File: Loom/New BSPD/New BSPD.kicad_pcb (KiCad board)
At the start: 2 copper layers, 148.6 x 83.8 mm, 54 parts, among them J1 Conn_01x03, J2 Conn_01x03, J3 Conn_01x03, J4 Screw_Terminal_01x02, K1 MCCMA51-S-DC12V-C, Q1 IRLZ44Z, U1 4011, U10 LM2901, U11 4012, U12 74LS573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

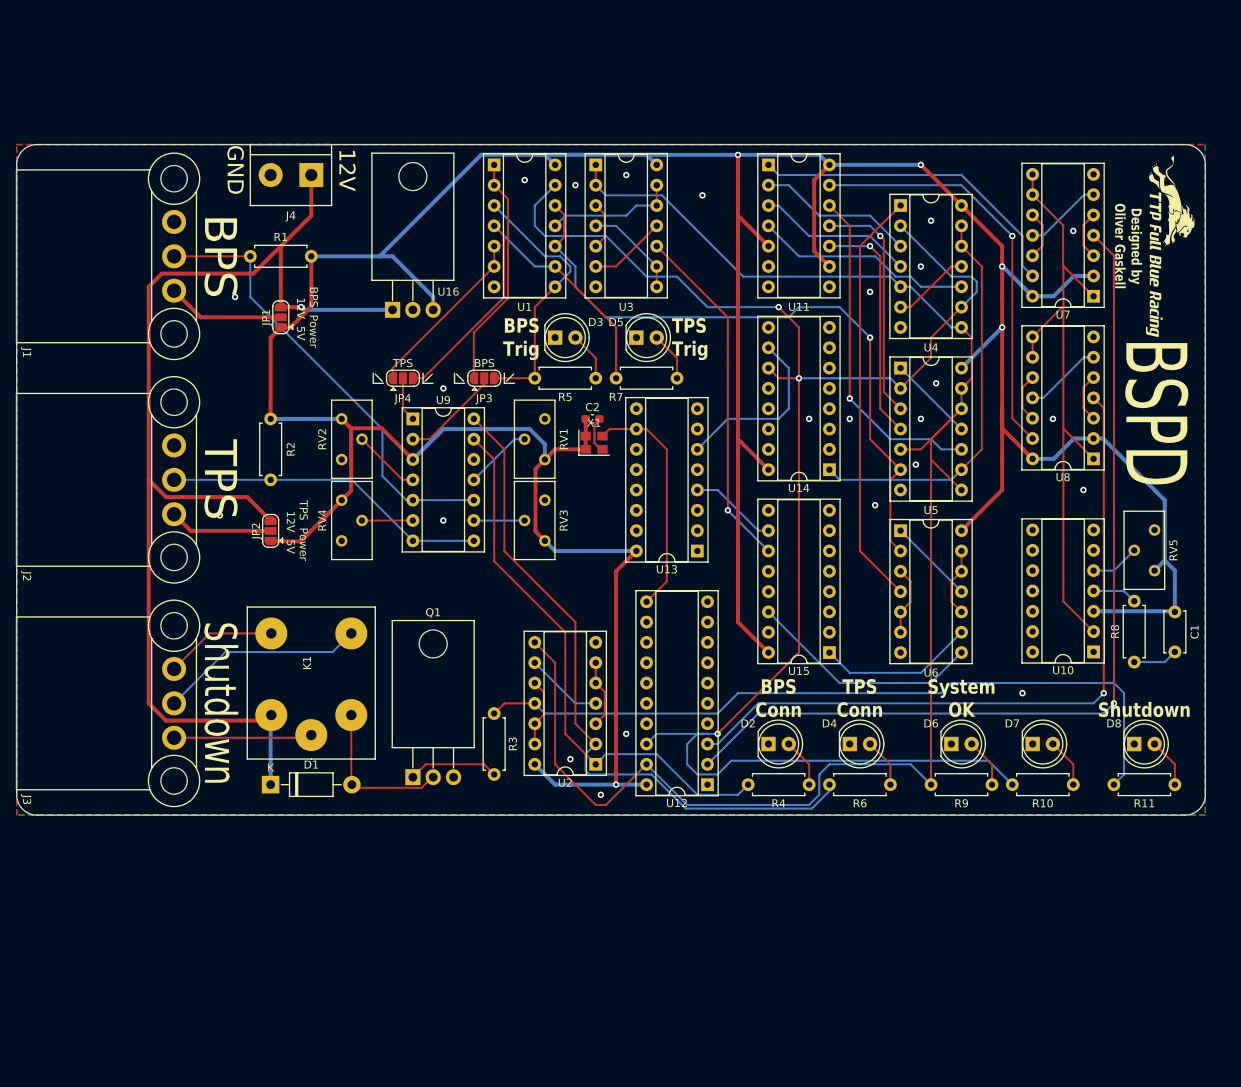
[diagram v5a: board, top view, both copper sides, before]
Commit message: Add mounting holes
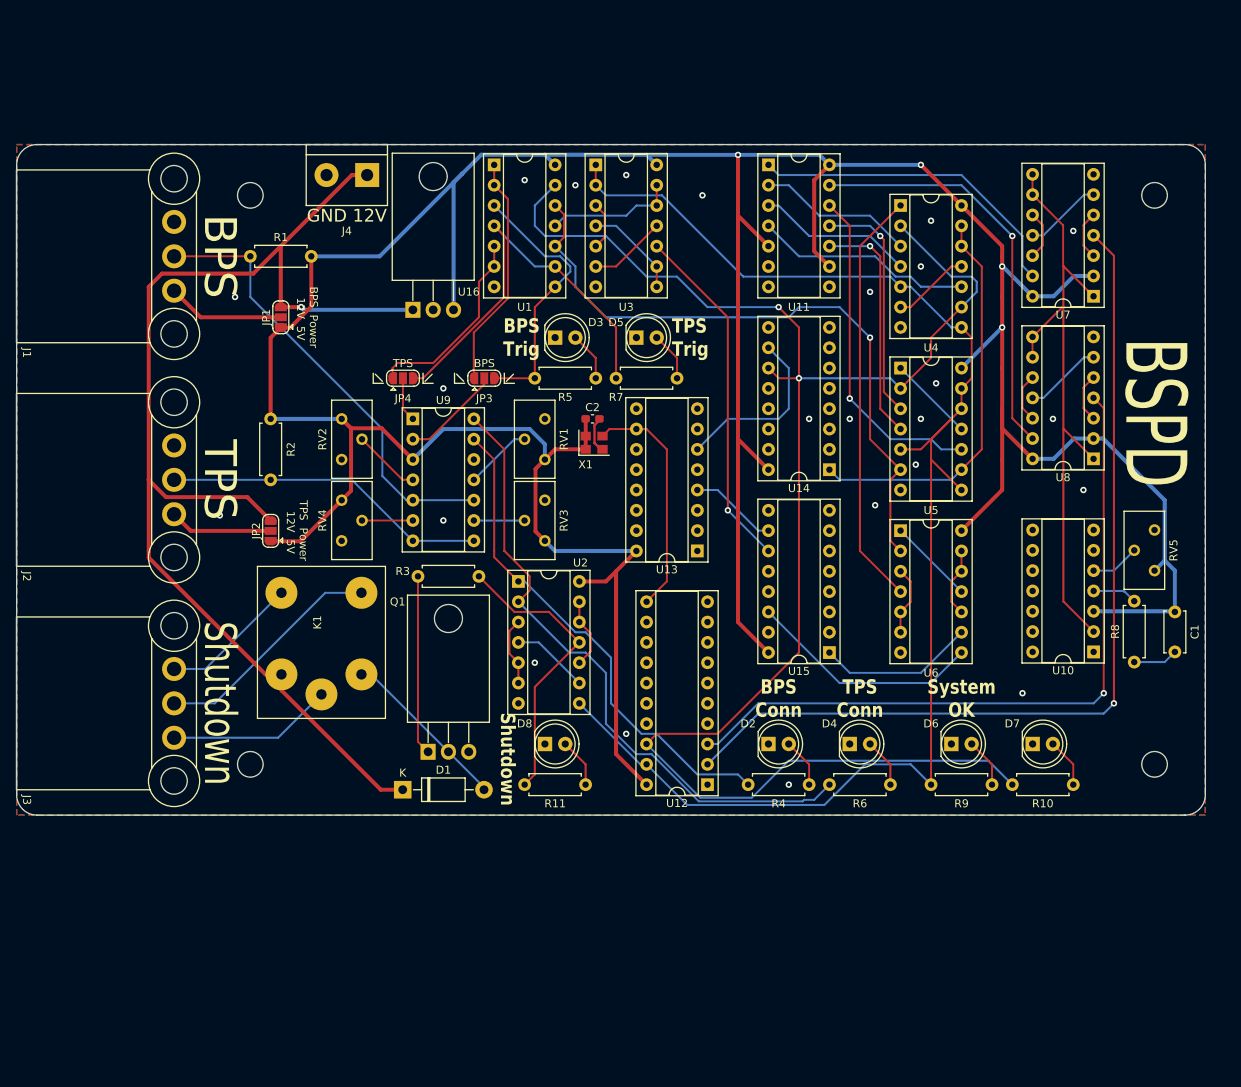
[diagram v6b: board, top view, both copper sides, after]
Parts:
- added MNT1: MountingHole_3.2mm_M3, MountingHole:MountingHole_3.2mm_M3, F.Cu at (194.3, 29.2)
- added MNT2: MountingHole_3.2mm_M3, MountingHole:MountingHole_3.2mm_M3, F.Cu at (194.3, 100.3)
- added MNT3: MountingHole_3.2mm_M3, MountingHole:MountingHole_3.2mm_M3, F.Cu at (81.3, 29.2)
- added MNT4: MountingHole_3.2mm_M3, MountingHole:MountingHole_3.2mm_M3, F.Cu at (81.3, 100.3)
- G***: moved to B.Cu
- moved D8 73.7 mm to (118.1, 97.8)
- moved R11 73.7 mm to (123.2, 102.9)
- moved U2 24.8 mm to (114.8, 77.5), turned to 0 degrees
- moved R3 17.3 mm to (109.9, 76.8), turned to 180 degrees
- moved D1 16.5 mm to (100.3, 103.5)
- moved G*** 16.1 mm to (191.8, 50.8)
- moved J4 6.98 mm to (95.9, 26.7)
- moved K1 5.24 mm to (90.2, 91.6)
- moved Q1 3.70 mm to (103.5, 98.8)
- moved U16 2.54 mm to (101.6, 43.5)
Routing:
- net /SD_Sig: track 93.9 -> 36.6 mm
- net /SM_Ok: track 203.0 -> 181.1 mm
- net Net-(Q1-G): track 11.4 -> 22.5 mm
- net +12V: track 146.0 -> 153.5 mm
- net /BPS_Plugged: track 69.2 -> 62.7 mm
- net /TPS_Plugged: track 85.0 -> 80.1 mm
- net /ShutdownNO: track 14.0 -> 17.4 mm
- net /ShutdownNC: track 25.8 -> 29.1 mm
- net /ShutdownC: track 17.3 -> 20.7 mm
- net /State Machine/State_B: track 204.8 -> 207.8 mm, vias 3 -> 2
- net Net-(JP4-A): track 21.8 -> 24.4 mm
- net Net-(D1-A): track 19.6 -> 21.5 mm
- net +5V: track 476.5 -> 475.2 mm, vias 5 -> 4
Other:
- board text added: "GND 12V"
- board text removed: "12V"
- board text removed: "GND"

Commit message: Add test points
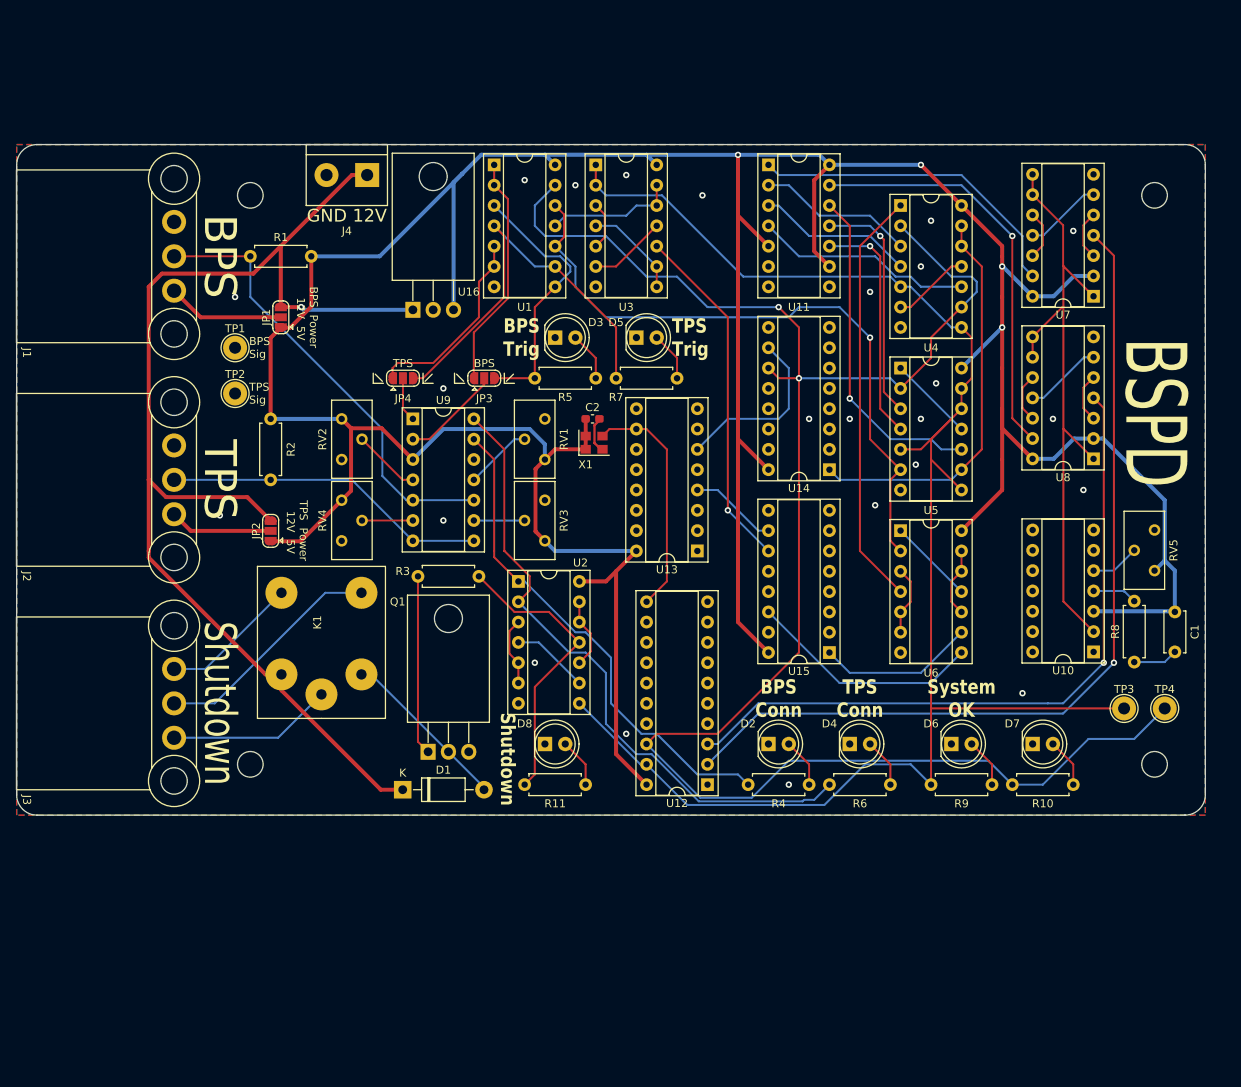
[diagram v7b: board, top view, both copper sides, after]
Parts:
- added TP1: TestPoint, TestPoint:TestPoint_THTPad_D3.0mm_Drill1.5mm, F.Cu at (79.4, 48.3)
- added TP2: TestPoint, TestPoint:TestPoint_THTPad_D3.0mm_Drill1.5mm, F.Cu at (79.4, 54.0)
- added TP3: TestPoint, TestPoint:TestPoint_THTPad_D3.0mm_Drill1.5mm, F.Cu at (190.5, 93.3)
- added TP4: TestPoint, TestPoint:TestPoint_THTPad_D3.0mm_Drill1.5mm, F.Cu at (195.6, 93.3)
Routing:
- net /SM_Ok: track 181.1 -> 205.2 mm
- net /State Machine/State_B: track 207.8 -> 230.8 mm
- net Net-(U12-D0): track 113.5 -> 110.5 mm
- net Net-(U12-D1): track 89.6 -> 87.4 mm
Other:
- board text added: "BPS Sig"
- board text added: "TPS Sig"

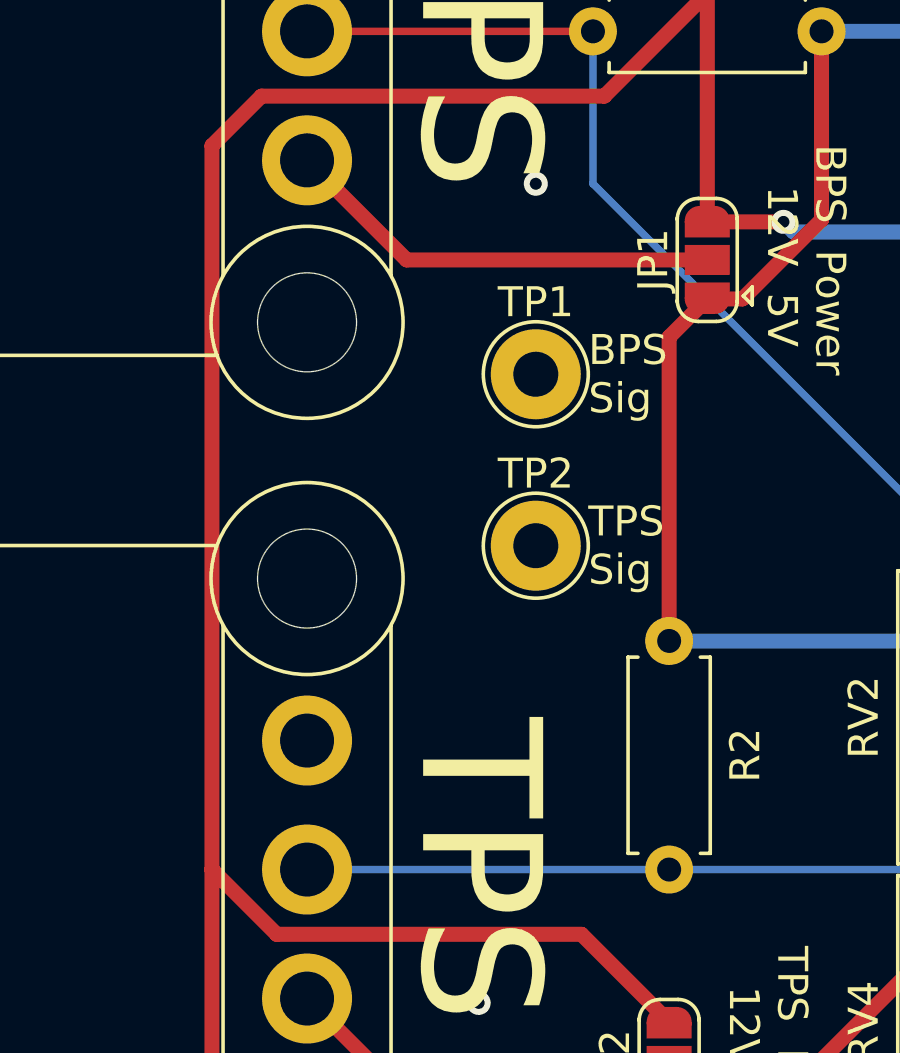
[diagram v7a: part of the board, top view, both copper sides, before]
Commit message: Fix BSPD Test Points
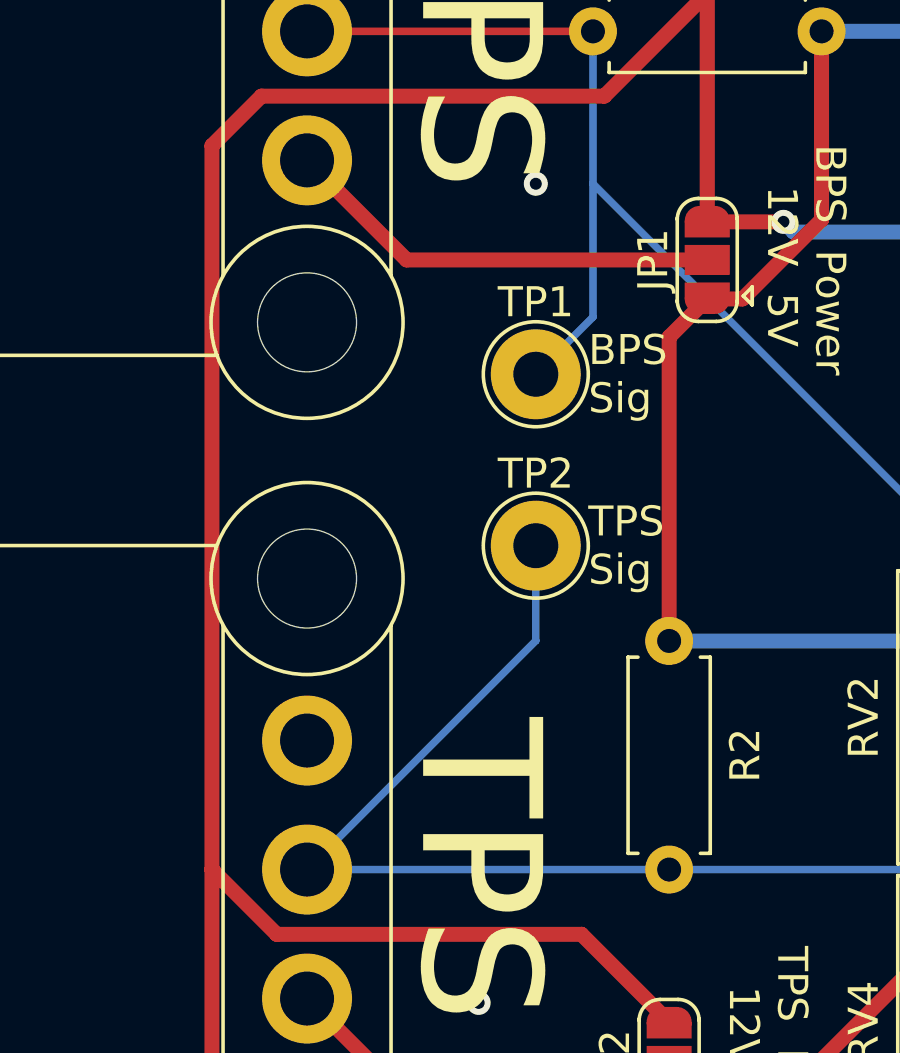
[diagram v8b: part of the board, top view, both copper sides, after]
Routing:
- net /TPS_Sig: track 40.6 -> 54.6 mm
- net /BPS_Sig: track 56.5 -> 63.7 mm
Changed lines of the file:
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@@
   (segment (start 101.6 67.31) (end 100.8 67.31) (width 0.25) (layer "B.Cu") (net 10))
   (segment (start 97.79 64.3) (end 97.79 58.42) (width 0.25) (layer "B.Cu") (net 10))
+  (segment (start 81.28 46.355) (end 79.375 48.26) (width 0.25) (layer "B.Cu") (net 10))
+  (segment (start 81.28 41.91) (end 81.28 46.355) (width 0.25) (layer "B.Cu") (net 10))
   (segment (start 97.79 58.42) (end 81.28 41.91) (width 0.25) (layer "B.Cu") (net 10))
   (segment (start 100.8 67.31) (end 97.79 64.3) (width 0.25) (layer "B.Cu") (net 10))
@@
   (segment (start 75.07 44.45) (end 85.09 44.45) (width 0.5) (layer "F.Cu") (net 11))
   (segment (start 109.22 72.39) (end 101.6 72.39) (width 0.25) (layer "B.Cu") (net 12))
+  (segment (start 79.375 53.975) (end 79.375 57.145) (width 0.25) (layer "B.Cu") (net 12))
+  (segment (start 79.375 57.145) (end 71.75 64.77) (width 0.25) (layer "B.Cu") (net 12))
   (segment (start 83.82 64.77) (end 93.98 64.77) (width 0.25) (layer "B.Cu") (net 12))
   (segment (start 83.82 64.77) (end 71.75 64.77) (width 0.25) (layer "B.Cu") (net 12))
